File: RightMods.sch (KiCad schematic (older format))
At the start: 13 parts

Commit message: Clean up some files
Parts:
- removed D42, D56, D63, D64: D_Small, Diodes_SMD:D_SOD-123, symbol D_Small
- removed RM1: MX-1.5U, MX_Alps_Hybrid:MX-1.5U, symbol MX-1U
- removed RM2, RM6: MX-1U, MX_Alps_Hybrid:MX-1U-FLIPPED, symbol MX-1U
- removed RM3, RM5: MX-1.25U, MX_Alps_Hybrid:MX-1.25U, symbol MX-1U
- removed RM4, RM7, RM9: MX-1U, MX_Alps_Hybrid:MX-1U, symbol MX-1U
- removed RM8: MX-1.5U, MX_Alps_Hybrid:MX-1.5U-FLIPPED, symbol MX-1U

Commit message: Replace MCU, route bus
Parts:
- added D69, D70, D71: D_Small, Diodes_SMD:D_SOD-123, symbol D_Small
- added K_RM1, K_RM4, K_RM6: MX-1U, MX_Alps_Hybrid:MX-1U, symbol MX-1U
- added K_RM2, K_RM5: MX-1.5U, MX_Alps_Hybrid:MX-1.5U, symbol MX-1U
- added K_RM3: MX-1.25U, MX_Alps_Hybrid:MX-1.25U, symbol MX-1U
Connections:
- new net: D69.2 (A), K_RM1.2 (ROW)
- new net: D70.2 (A), K_RM3.2 (ROW)
- new net: D71.2 (A), K_RM5.2 (ROW)
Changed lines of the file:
@@
 $Descr A4 11693 8268
 encoding utf-8
-Sheet 5 6
+Sheet 4 6
 Title ""
 Date ""
@@
 Comment4 ""
 $EndDescr
+$Comp
+L MX-1U K_RM1
+U 1 1 5ACDE9C4
+P 2000 2000
+F 0 "K_RM1" H 2000 2125 60  0000 C CNN
+F 1 "MX-1U" H 2000 2050 20  0000 C CNN
+F 2 "MX_Alps_Hybrid:MX-1U" H 1975 1975 60  0001 C CNN
+F 3 "" H 1975 1975 60  0001 C CNN
+	1    2000 2000
+	1    0    0    -1
+$EndComp
+$Comp
+L MX-1U K_RM2
+U 1 1 5ACDEF3B
+P 2000 2700
+F 0 "K_RM2" H 2000 2825 60  0000 C CNN
+F 1 "MX-1.5U" H 2000 2750 20  0000 C CNN
+F 2 "MX_Alps_Hybrid:MX-1.5U" H 1975 2675 60  0001 C CNN
+F 3 "" H 1975 2675 60  0001 C CNN
+	1    2000 2700
+	1    0    0    -1
+$EndComp
+$Comp
+L D_Small D69
+U 1 1 5ACDEF6C
+P 1900 2275
+F 0 "D69" H 1850 2355 50  0000 L CNN
+F 1 "D_Small" H 1750 2195 50  0000 L CNN
+F 2 "Diodes_SMD:D_SOD-123" V 1900 2275 50  0001 C CNN
+F 3 "" V 1900 2275 50  0001 C CNN
+	1    1900 2275
+	0    -1   -1   0
+$EndComp
+$Comp
+L MX-1U K_RM3
+U 1 1 5ACDF27C
+P 2625 2000
+F 0 "K_RM3" H 2625 2125 60  0000 C CNN
+F 1 "MX-1.25U" H 2625 2050 20  0000 C CNN
+F 2 "MX_Alps_Hybrid:MX-1.25U" H 2600 1975 60  0001 C CNN
+F 3 "" H 2600 1975 60  0001 C CNN
+	1    2625 2000
+	1    0    0    -1
+$EndComp
+$Comp
+L D_Small D70
+U 1 1 5ACDF282
+P 2525 2275
+F 0 "D70" H 2475 2355 50  0000 L CNN
+F 1 "D_Small" H 2375 2195 50  0000 L CNN
+F 2 "Diodes_SMD:D_SOD-123" V 2525 2275 50  0001 C CNN
+F 3 "" V 2525 2275 50  0001 C CNN
+	1    2525 2275
+	0    -1   -1   0
+$EndComp
+$Comp
+L MX-1U K_RM4
+U 1 1 5ACDF2B5
+P 2625 2700
+F 0 "K_RM4" H 2625 2825 60  0000 C CNN
+F 1 "MX-1U" H 2625 2750 20  0000 C CNN
+F 2 "MX_Alps_Hybrid:MX-1U" H 2600 2675 60  0001 C CNN
+F 3 "" H 2600 2675 60  0001 C CNN
+	1    2625 2700
+	1    0    0    -1
+$EndComp
+$Comp
+L MX-1U K_RM5
+U 1 1 5ACDF5EF
+P 3325 2000
+F 0 "K_RM5" H 3325 2125 60  0000 C CNN
+F 1 "MX-1.5U" H 3325 2050 20  0000 C CNN
+F 2 "MX_Alps_Hybrid:MX-1.5U" H 3300 1975 60  0001 C CNN
+F 3 "" H 3300 1975 60  0001 C CNN
+	1    3325 2000
+	1    0    0    -1
+$EndComp
+$Comp
+L MX-1U K_RM6
+U 1 1 5ACDF5F5
+P 3325 2700
+F 0 "K_RM6" H 3325 2825 60  0000 C CNN
+F 1 "MX-1U" H 3325 2750 20  0000 C CNN
+F 2 "MX_Alps_Hybrid:MX-1U" H 3300 2675 60  0001 C CNN
+F 3 "" H 3300 2675 60  0001 C CNN
+	1    3325 2700
+	1    0    0    -1
+$EndComp
+$Comp
+L D_Small D71
+U 1 1 5ACDF5FB
+P 3225 2275
+F 0 "D71" H 3175 2355 50  0000 L CNN
+F 1 "D_Small" H 3075 2195 50  0000 L CNN
+F 2 "Diodes_SMD:D_SOD-123" V 3225 2275 50  0001 C CNN
+F 3 "" V 3225 2275 50  0001 C CNN
+	1    3225 2275
+	0    -1   -1   0
+$EndComp
+Wire Wire Line
+	1900 2175 1975 2175
+Wire Wire Line
+	2525 2175 2600 2175
+Wire Wire Line
+	3225 2175 3300 2175
 $EndSCHEMATC

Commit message: Temporary progress save
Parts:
- K_RM2: footprint MX_Alps_Hybrid:MX-1.5U -> MX_Alps_Hybrid:MX-1.5U-FLIPPED
- K_RM4, K_RM6: footprint MX_Alps_Hybrid:MX-1U -> MX_Alps_Hybrid:MX-1U-FLIPPED
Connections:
- net COL10: now reaches K_RM1.1 (COL)
- net COL10: now also K_RM2.2 (ROW)
- net at D69.2 (A), K_RM1.2 (ROW): now also K_RM2.1 (COL)
- net ROW4: now reaches D69.1 (K)
- net ROW4: now also D70.1 (K), D71.1 (K)
- net COL11: now reaches K_RM3.1 (COL)
- net COL11: now also K_RM4.1 (COL)
- net at D70.2 (A), K_RM3.2 (ROW): now also K_RM4.2 (ROW)
- net COL12: now reaches K_RM5.1 (COL)
- net COL12: now also K_RM6.2 (ROW)
- net at D71.2 (A), K_RM5.2 (ROW): now also K_RM6.1 (COL)
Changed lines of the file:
@@
 F 0 "K_RM2" H 2000 2825 60  0000 C CNN
 F 1 "MX-1.5U" H 2000 2750 20  0000 C CNN
-F 2 "MX_Alps_Hybrid:MX-1.5U" H 1975 2675 60  0001 C CNN
+F 2 "MX_Alps_Hybrid:MX-1.5U-FLIPPED" H 1975 2675 60  0001 C CNN
 F 3 "" H 1975 2675 60  0001 C CNN
 	1    2000 2700
@@
 F 0 "K_RM4" H 2625 2825 60  0000 C CNN
 F 1 "MX-1U" H 2625 2750 20  0000 C CNN
-F 2 "MX_Alps_Hybrid:MX-1U" H 2600 2675 60  0001 C CNN
+F 2 "MX_Alps_Hybrid:MX-1U-FLIPPED" H 2600 2675 60  0001 C CNN
 F 3 "" H 2600 2675 60  0001 C CNN
 	1    2625 2700
@@
 F 0 "K_RM6" H 3325 2825 60  0000 C CNN
 F 1 "MX-1U" H 3325 2750 20  0000 C CNN
-F 2 "MX_Alps_Hybrid:MX-1U" H 3300 2675 60  0001 C CNN
+F 2 "MX_Alps_Hybrid:MX-1U-FLIPPED" H 3300 2675 60  0001 C CNN
 F 3 "" H 3300 2675 60  0001 C CNN
 	1    3325 2700
@@
 $EndComp
 Wire Wire Line
-	1900 2175 1975 2175
+	1900 2175 2325 2175
 Wire Wire Line
 	2525 2175 2600 2175
 Wire Wire Line
-	3225 2175 3300 2175
+	3225 2175 3675 2175
+Wire Wire Line
+	3500 1400 3500 2475
+Connection ~ 3500 1975
+Text GLabel 3500 1400 1    60   Input ~ 0
+COL12
+Wire Wire Line
+	2800 1400 2800 2675
+Connection ~ 2800 1975
+Text GLabel 2800 1400 1    60   Input ~ 0
+COL11
+Wire Wire Line
+	2175 1400 2175 2475
+Connection ~ 2175 1975
+Text GLabel 2175 1400 1    60   Input ~ 0
+COL10
+Wire Wire Line
+	1500 2375 3225 2375
+Connection ~ 2525 2375
+Connection ~ 1900 2375
+Text GLabel 1500 2375 0    60   Input ~ 0
+ROW4
+Wire Wire Line
+	3500 2475 3300 2475
+Wire Wire Line
+	3300 2475 3300 2875
+Wire Wire Line
+	3500 2675 3675 2675
+Wire Wire Line
+	3675 2675 3675 2175
+Connection ~ 3300 2175
+Wire Wire Line
+	2175 2475 1975 2475
+Wire Wire Line
+	1975 2475 1975 2875
+Wire Wire Line
+	2175 2675 2325 2675
+Wire Wire Line
+	2325 2675 2325 2175
+Connection ~ 1975 2175
+Wire Wire Line
+	2600 2175 2600 2875
 $EndSCHEMATC

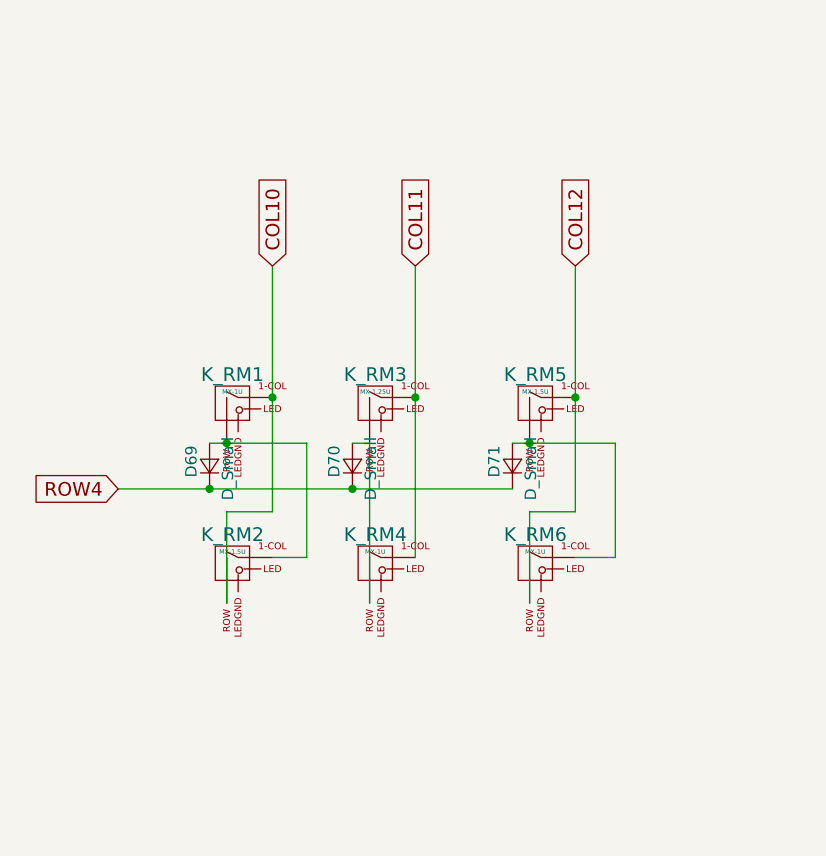
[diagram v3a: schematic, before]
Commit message: Finish project basic routing
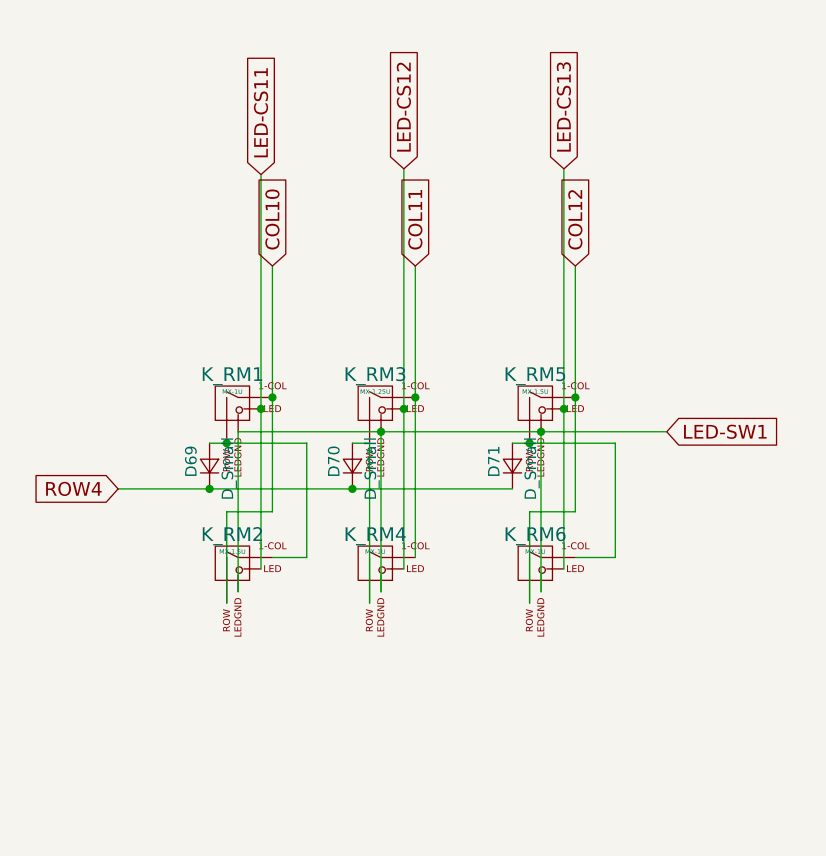
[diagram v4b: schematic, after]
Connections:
- net LED-CS11: now reaches K_RM1.3 (LED)
- net LED-CS11: now also K_RM2.3 (LED)
- net LED-SW1: now reaches K_RM1.4 (LEDGND)
- net LED-SW1: now also K_RM2.4 (LEDGND), K_RM3.4 (LEDGND), K_RM4.4 (LEDGND), K_RM5.4 (LEDGND), K_RM6.4 (LEDGND)
- net LED-CS12: now reaches K_RM3.3 (LED)
- net LED-CS12: now also K_RM4.3 (LED)
- net LED-CS13: now reaches K_RM5.3 (LED)
- net LED-CS13: now also K_RM6.3 (LED)
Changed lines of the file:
@@
 	0    -1   -1   0
 $EndComp
+Text GLabel 3500 1400 1    60   Input ~ 0
+COL12
+Text GLabel 2800 1400 1    60   Input ~ 0
+COL11
+Text GLabel 2175 1400 1    60   Input ~ 0
+COL10
+Text GLabel 1500 2375 0    60   Input ~ 0
+ROW4
 Wire Wire Line
 	1900 2175 2325 2175
@@
 	3500 1400 3500 2475
 Connection ~ 3500 1975
-Text GLabel 3500 1400 1    60   Input ~ 0
-COL12
 Wire Wire Line
 	2800 1400 2800 2675
 Connection ~ 2800 1975
-Text GLabel 2800 1400 1    60   Input ~ 0
-COL11
 Wire Wire Line
 	2175 1400 2175 2475
 Connection ~ 2175 1975
-Text GLabel 2175 1400 1    60   Input ~ 0
-COL10
 Wire Wire Line
 	1500 2375 3225 2375
 Connection ~ 2525 2375
 Connection ~ 1900 2375
-Text GLabel 1500 2375 0    60   Input ~ 0
-ROW4
 Wire Wire Line
 	3500 2475 3300 2475
@@
 Wire Wire Line
 	2600 2175 2600 2875
+Wire Wire Line
+	2125 1000 2125 2725
+Text GLabel 2125 1000 1    60   Input ~ 0
+LED-CS11
+Wire Wire Line
+	2750 975  2750 2725
+Connection ~ 2750 2025
+Text GLabel 2750 975  1    60   Input ~ 0
+LED-CS12
+Wire Wire Line
+	3450 975  3450 2725
+Text GLabel 3450 975  1    60   Input ~ 0
+LED-CS13
+Connection ~ 3450 2025
+Wire Wire Line
+	2025 2125 3900 2125
+Text GLabel 3900 2125 2    60   Input ~ 0
+LED-SW1
+Connection ~ 3350 2125
+Connection ~ 2650 2125
+Wire Wire Line
+	2025 2125 2025 2825
+Wire Wire Line
+	2650 2825 2650 2125
+Wire Wire Line
+	3350 2125 3350 2825
+Connection ~ 2125 2025
 $EndSCHEMATC

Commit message: Low cost edition complete
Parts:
- K_RM1: footprint MX_Alps_Hybrid:MX-1U -> MX_Alps_Hybrid:MX-1U-NoLED
- K_RM2: footprint MX_Alps_Hybrid:MX-1.5U-FLIPPED -> MX_Alps_Hybrid:MX-1.5U-NoLED
- K_RM3: footprint MX_Alps_Hybrid:MX-1.25U -> MX_Alps_Hybrid:MX-1.25U-NoLED
- K_RM4, K_RM6: footprint MX_Alps_Hybrid:MX-1U-FLIPPED -> MX_Alps_Hybrid:MX-1U-NoLED
- K_RM5: footprint MX_Alps_Hybrid:MX-1.5U -> MX_Alps_Hybrid:MX-1.5U-NoLED
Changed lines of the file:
@@
 F 0 "K_RM1" H 2000 2125 60  0000 C CNN
 F 1 "MX-1U" H 2000 2050 20  0000 C CNN
-F 2 "MX_Alps_Hybrid:MX-1U" H 1975 1975 60  0001 C CNN
+F 2 "MX_Alps_Hybrid:MX-1U-NoLED" H 1975 1975 60  0001 C CNN
 F 3 "" H 1975 1975 60  0001 C CNN
 	1    2000 2000
@@
 F 0 "K_RM2" H 2000 2825 60  0000 C CNN
 F 1 "MX-1.5U" H 2000 2750 20  0000 C CNN
-F 2 "MX_Alps_Hybrid:MX-1.5U-FLIPPED" H 1975 2675 60  0001 C CNN
+F 2 "MX_Alps_Hybrid:MX-1.5U-NoLED" H 1975 2675 60  0001 C CNN
 F 3 "" H 1975 2675 60  0001 C CNN
 	1    2000 2700
@@
 F 0 "K_RM3" H 2625 2125 60  0000 C CNN
 F 1 "MX-1.25U" H 2625 2050 20  0000 C CNN
-F 2 "MX_Alps_Hybrid:MX-1.25U" H 2600 1975 60  0001 C CNN
+F 2 "MX_Alps_Hybrid:MX-1.25U-NoLED" H 2600 1975 60  0001 C CNN
 F 3 "" H 2600 1975 60  0001 C CNN
 	1    2625 2000
@@
 F 0 "K_RM4" H 2625 2825 60  0000 C CNN
 F 1 "MX-1U" H 2625 2750 20  0000 C CNN
-F 2 "MX_Alps_Hybrid:MX-1U-FLIPPED" H 2600 2675 60  0001 C CNN
+F 2 "MX_Alps_Hybrid:MX-1U-NoLED" H 2600 2675 60  0001 C CNN
 F 3 "" H 2600 2675 60  0001 C CNN
 	1    2625 2700
@@
 F 0 "K_RM5" H 3325 2125 60  0000 C CNN
 F 1 "MX-1.5U" H 3325 2050 20  0000 C CNN
-F 2 "MX_Alps_Hybrid:MX-1.5U" H 3300 1975 60  0001 C CNN
+F 2 "MX_Alps_Hybrid:MX-1.5U-NoLED" H 3300 1975 60  0001 C CNN
 F 3 "" H 3300 1975 60  0001 C CNN
 	1    3325 2000
@@
 F 0 "K_RM6" H 3325 2825 60  0000 C CNN
 F 1 "MX-1U" H 3325 2750 20  0000 C CNN
-F 2 "MX_Alps_Hybrid:MX-1U-FLIPPED" H 3300 2675 60  0001 C CNN
+F 2 "MX_Alps_Hybrid:MX-1U-NoLED" H 3300 2675 60  0001 C CNN
 F 3 "" H 3300 2675 60  0001 C CNN
 	1    3325 2700
